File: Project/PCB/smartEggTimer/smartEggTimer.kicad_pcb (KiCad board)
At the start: 2 copper layers, 72 x 72 mm, 64 parts, among them J1 Conn_01x05_Pin, J2 Conn_01x02_Pin, J3 Conn_01x02_Pin, J4 Conn_01x06_Pin, J5 Conn_01x02_Socket, J6 Conn_01x02_Socket, J7 Conn_01x03_Pin, J8 Conn_01x03_Pin, Q1 STP60NF06L, SW1 SW_Push_Dual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

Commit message: rough positioning
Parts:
- C10, C11: footprint Capacitor_SMD:C_0603_1608Metric -> Capacitor_SMD:C_0805_2012Metric
- C12, C13, C7: footprint Capacitor_SMD:C_0805_2012Metric -> Capacitor_SMD:C_0402_1005Metric
- C15, C16, C17, C18, C8, C9: footprint Capacitor_SMD:C_0603_1608Metric -> Capacitor_SMD:C_0402_1005Metric
- SW1: value SW_Push_Dual -> SW_Push; footprint Button_Switch_THT:SW_PUSH_6mm_H9.5mm -> Button_Switch_THT:SW_PUSH_6mm
- SW3, SW4, SW5, SW6: value SW_Push_Dual -> SW_Push
- moved C14 105.4 mm to (125.6, 83.4), turned to -90 degrees
- moved C4 98.0 mm to (128.5, 91.4), turned to 90 degrees
- moved R14 97.7 mm to (121.4, 90.5)
- moved R12 97.5 mm to (124.5, 81.1), turned to 180 degrees
- moved R13 96.7 mm to (126.6, 81.1), turned to 180 degrees
- moved R15 96.6 mm to (121.5, 96.5), turned to 180 degrees
- moved C2 95.6 mm to (128.6, 97.4), turned to 90 degrees
- moved C5 89.1 mm to (140.3, 86.6)
- moved R17 87.0 mm to (129.7, 112.4), turned to -90 degrees
- moved C6 85.7 mm to (143.2, 90.4), turned to -90 degrees
- moved C3 84.5 mm to (139.5, 101.4), turned to 180 degrees
- moved C7 83.2 mm to (134.2, 86.5)
- moved R3 80.5 mm to (130.7, 82.1), turned to -90 degrees
- moved R16 80.2 mm to (136.3, 112.4), turned to 90 degrees
- moved C15 76.5 mm to (121.5, 97.7), turned to 180 degrees
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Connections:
- DFPlayerMini1 pad 3: /UART2_TX -> /USART2_RX
- J1 pad 3: /I2C_SCL -> /I2C1_SCL
- J3 pad 1: unconnected-(J3-Pin_1-Pad1) -> /USART3_TX
- J3 pad 2: unconnected-(J3-Pin_2-Pad2) -> /USART3_RX
- J4 pad 4: /I2C_SCL -> /I2C1_SCL
- OLED-15W-C1 pad 4: /I2C_SCL -> /I2C1_SCL
- R15 pad 2: Net-(R15-Pad2) -> Net-(R14-Pad1)
- R17 pad 2: Net-(R17-Pad2) -> Net-(R16-Pad1)
- R19 pad 2: Net-(R19-Pad2) -> Net-(R18-Pad1)
- R21 pad 2: Net-(R21-Pad2) -> Net-(R20-Pad1)
- R3 pad 2: /UART2_RX -> /USART2_TX
- R6 pad 1: /I2C1_SDA -> /I2C1_SCL
- R7 pad 1: /I2C_SCL -> /I2C1_SDA
- SW1 pad 1: /NRST -> GND
- SW3 pad 1: Net-(R14-Pad1) -> GND
- SW3 pad 2: Net-(R15-Pad2) -> Net-(R14-Pad1)
- SW4 pad 1: Net-(R16-Pad1) -> GND
- SW4 pad 2: Net-(R17-Pad2) -> Net-(R16-Pad1)
- SW5 pad 1: Net-(R18-Pad1) -> GND
- SW5 pad 2: Net-(R19-Pad2) -> Net-(R18-Pad1)
- SW6 pad 1: Net-(R20-Pad1) -> GND
- SW6 pad 2: Net-(R21-Pad2) -> Net-(R20-Pad1)
- U1 pad 16: unconnected-(U1-PA2-Pad16) -> /USART2_TX
- U1 pad 17: /UART2_RX -> /USART2_RX
- U1 pad 20: /UART2_TX -> unconnected-(U1-PA4-Pad20)
- U1 pad 51: unconnected-(U1-PC10-Pad51) -> /USART3_TX
- U1 pad 52: unconnected-(U1-PC11-Pad52) -> /USART3_RX
- U1 pad 58: /I2C1_SDA -> /I2C1_SCL
- U1 pad 59: /I2C_SCL -> /I2C1_SDA

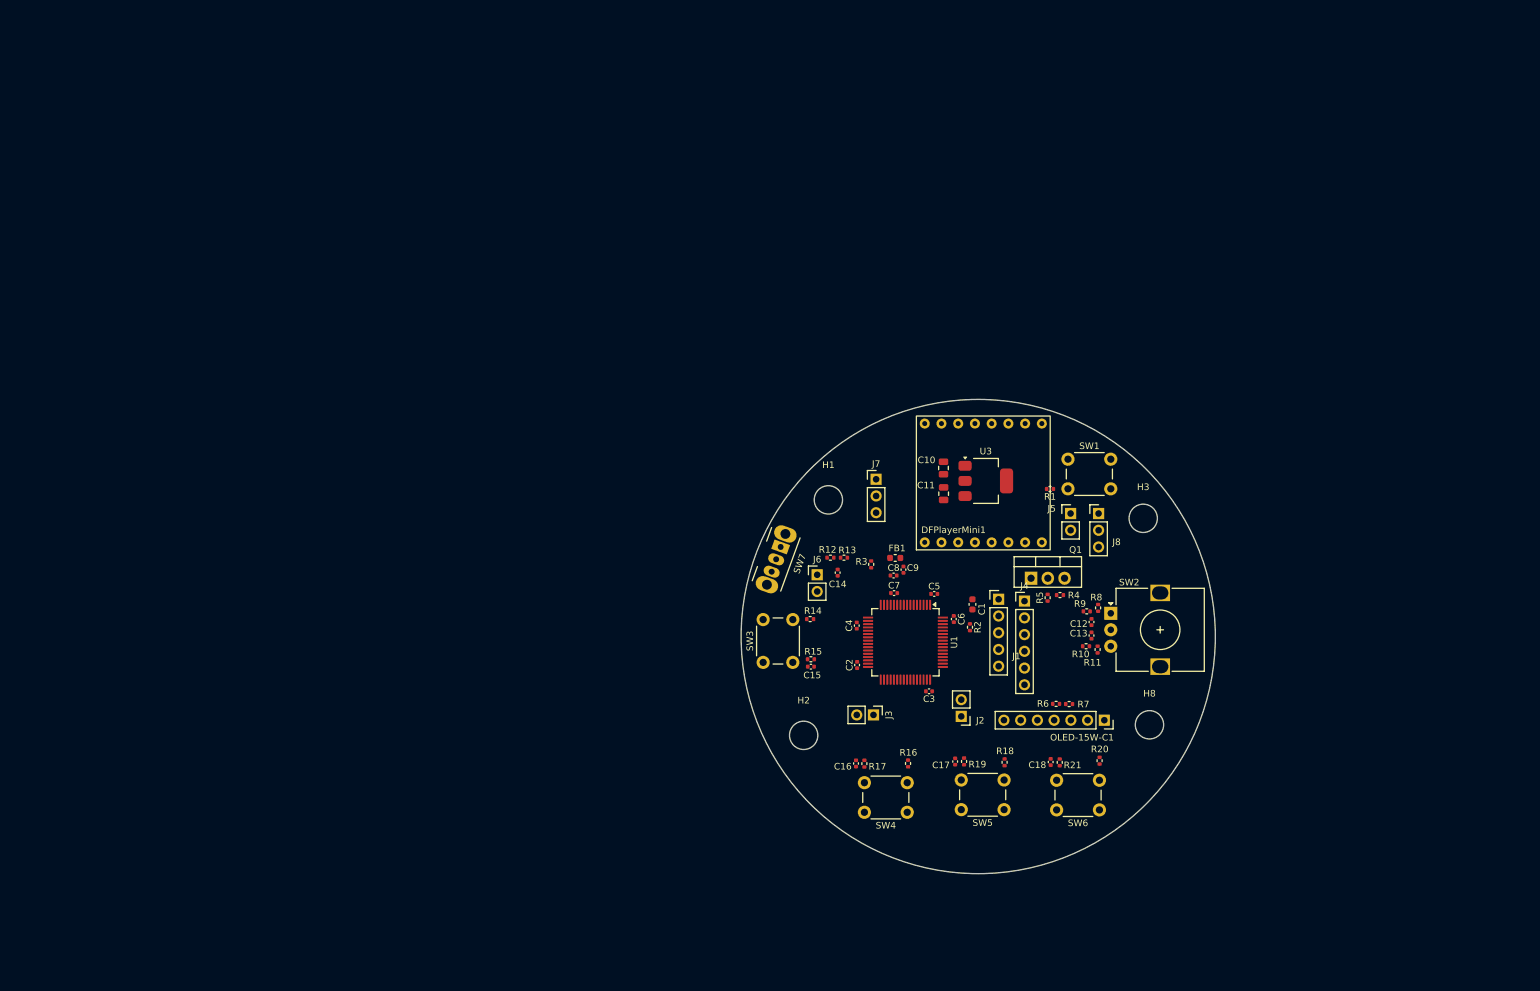
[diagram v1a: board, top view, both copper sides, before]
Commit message: add GND pins for SWD and optional UART
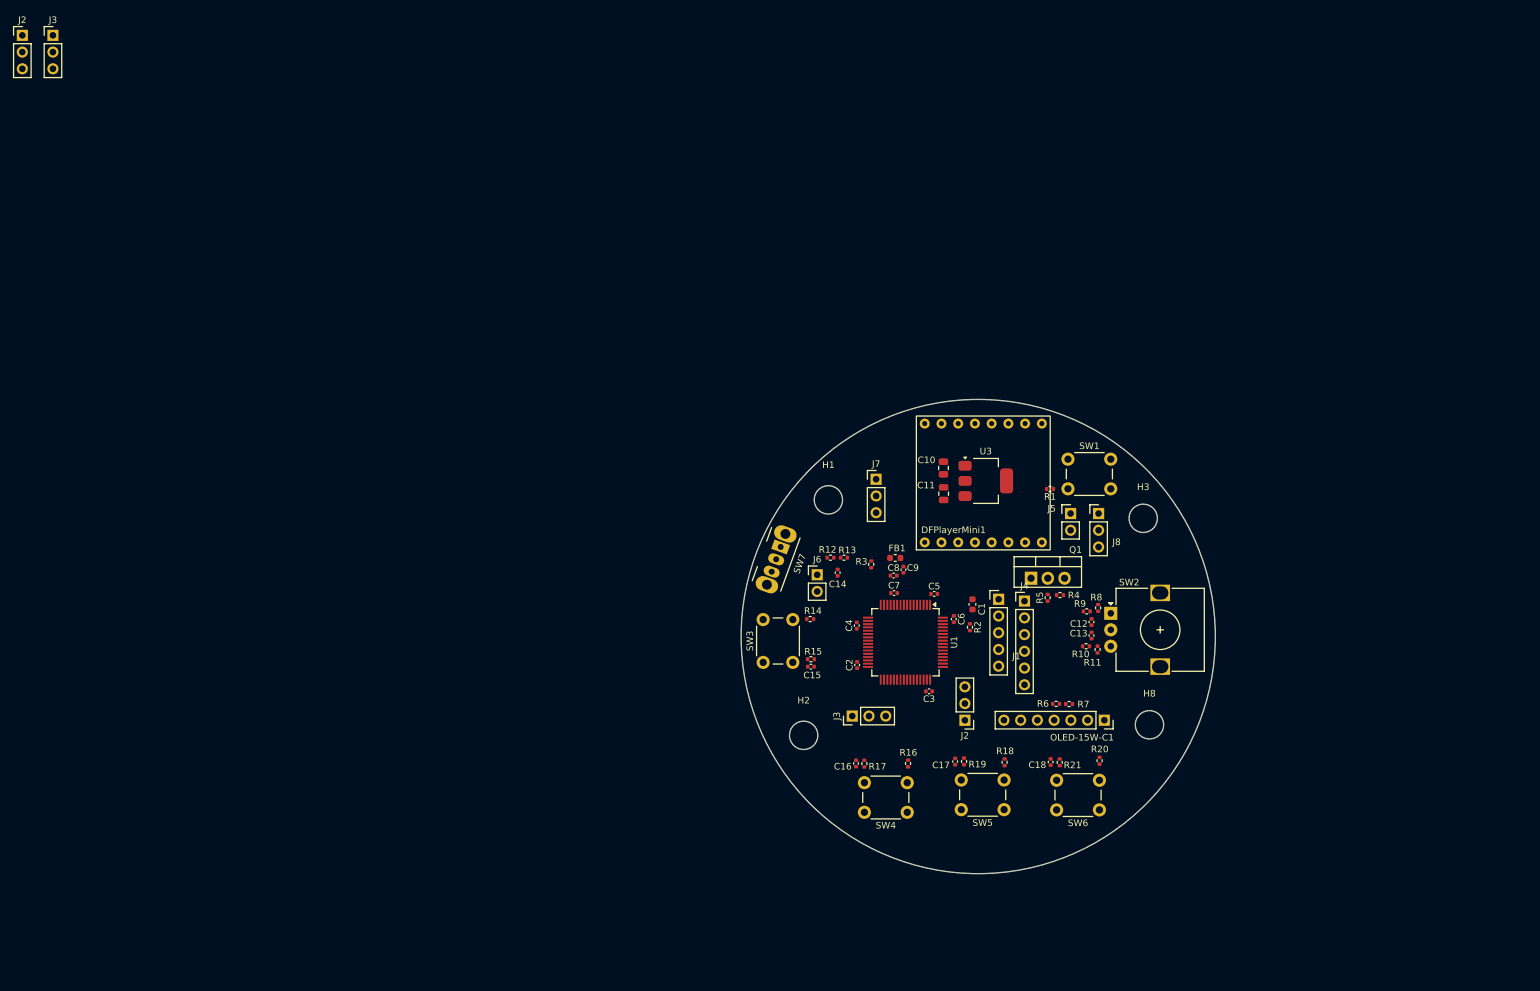
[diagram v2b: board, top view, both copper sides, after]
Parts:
- added J2: Conn_01x03_Pin, Connector_PinHeader_2.54mm:PinHeader_1x03_P2.54mm_Vertical, F.Cu at (1.82, 1.82)
- added J3: Conn_01x03_Pin, Connector_PinHeader_2.54mm:PinHeader_1x03_P2.54mm_Vertical, F.Cu at (6.47, 1.82)
- J2, J3: value Conn_01x02_Pin -> Conn_01x03_Pin; footprint Connector_PinHeader_2.54mm:PinHeader_1x02_P2.54mm_Vertical -> Connector_PinHeader_2.54mm:PinHeader_1x03_P2.54mm_Vertical
- moved J3 3.23 mm to (127.8, 105.2), turned to 90 degrees
- moved J2 0.81 mm to (144.9, 105.8)

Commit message: add exact positioning of critical parts (switches, rotary encoder and drill holes need to fit to the 3D design of the case)
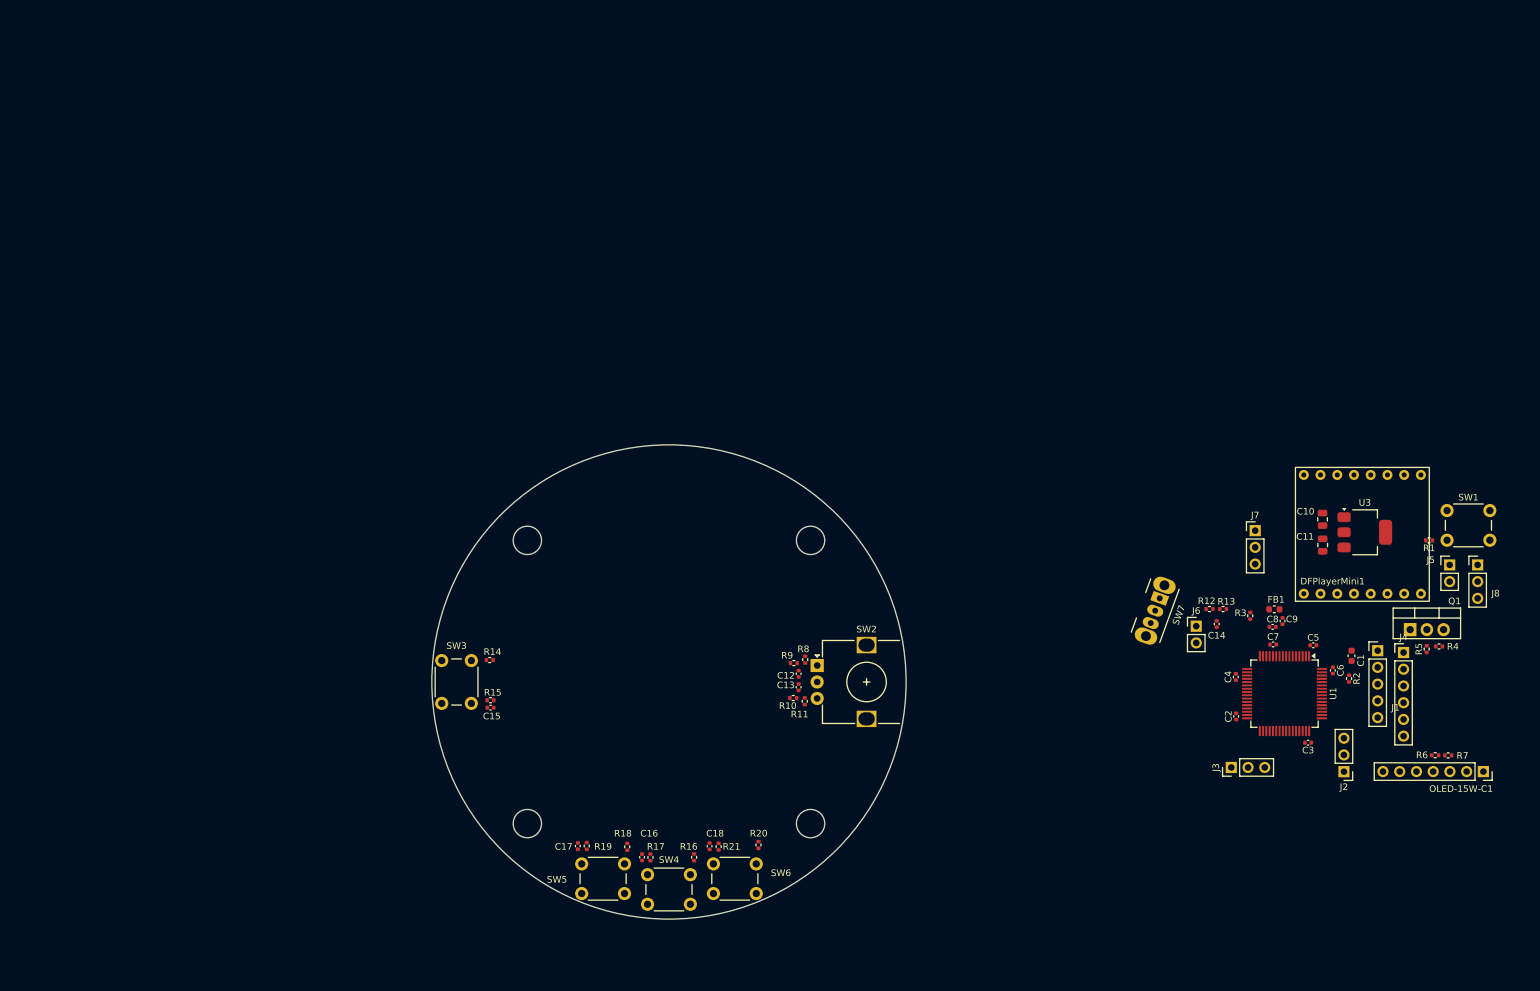
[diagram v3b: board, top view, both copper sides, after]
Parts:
- removed the J2 at (1.82, 1.82)
- removed the J3 at (6.47, 1.82)
- moved H3 104.4 mm to (78.5, 121.5)
- moved SW5 61.8 mm to (90.0, 129.9)
- moved R18 58.7 mm to (93.7, 125.0)
- moved R19 58.7 mm to (87.5, 124.9)
- moved C17 58.7 mm to (86.2, 124.9)
- moved C1 58.1 mm to (203.6, 96.0)
- moved C11 58.1 mm to (199.2, 79.2)
- moved C2 58.1 mm to (186.1, 105.2)
- moved C3 58.1 mm to (197.0, 109.2)
- moved C4 58.1 mm to (186.1, 99.2)
- moved C5 58.1 mm to (197.8, 94.4)
- moved C6 58.1 mm to (200.8, 98.2)
- moved C7 58.1 mm to (191.7, 94.3)
- moved C8 58.1 mm to (191.7, 91.6)
- moved C9 58.1 mm to (193.2, 90.7)
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
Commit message: rework DFPlayer section based on prototyping - add pull-up resistors for UART communication - add a pin header for the input voltage
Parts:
- removed R3: 1k, Resistor_SMD:R_0402_1005Metric
- added J9: Conn_01x02_Pin, Connector_PinHeader_2.54mm:PinHeader_1x02_P2.54mm_Vertical, F.Cu at (224.7, 104.3)
- added R22: 100k, Resistor_SMD:R_0402_1005Metric, F.Cu at (228.5, 103.0)
- added R23: 100k, Resistor_SMD:R_0402_1005Metric, F.Cu at (228.5, 105.0)
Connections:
- DFPlayerMini1 pad 1: /Battery-SW -> Net-(DFPlayerMini1-VCC)
- DFPlayerMini1 pad 2: Net-(DFPlayerMini1-RX) -> /USART2_TX

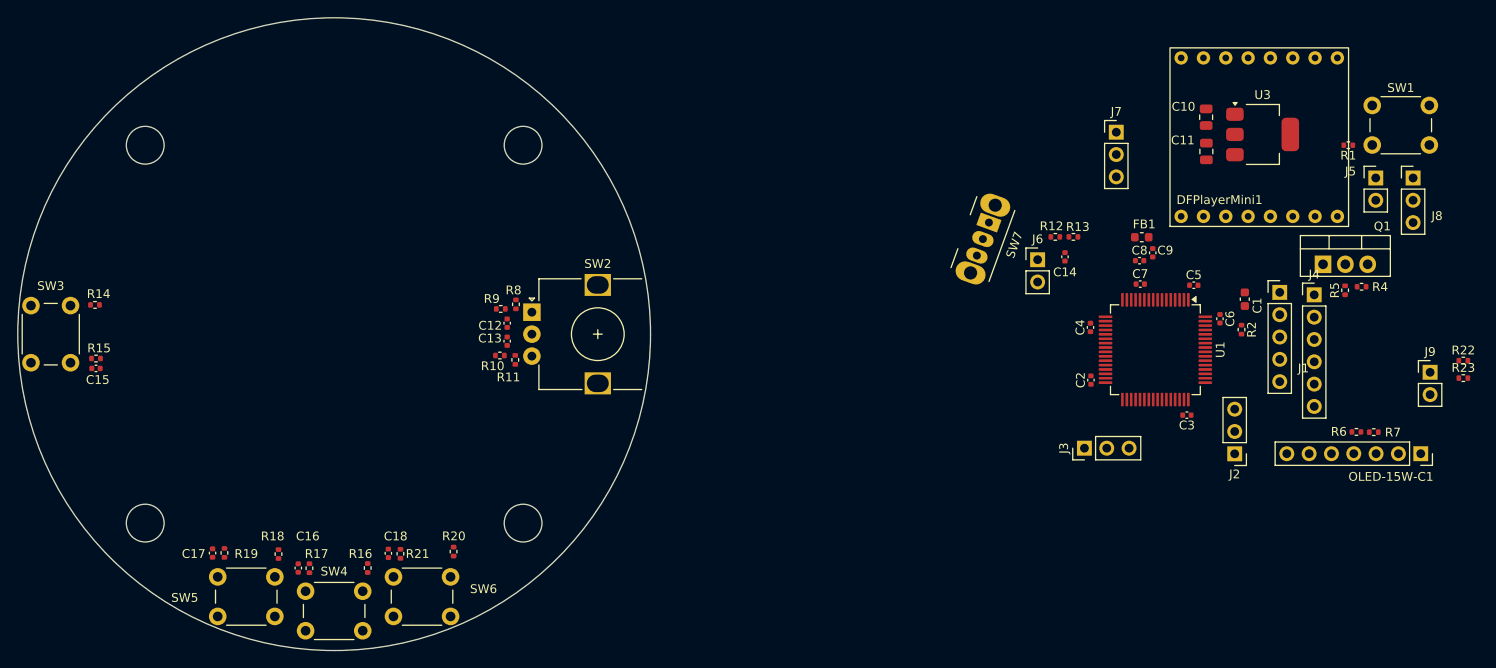
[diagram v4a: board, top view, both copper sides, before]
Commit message: placement of all components & initial routing
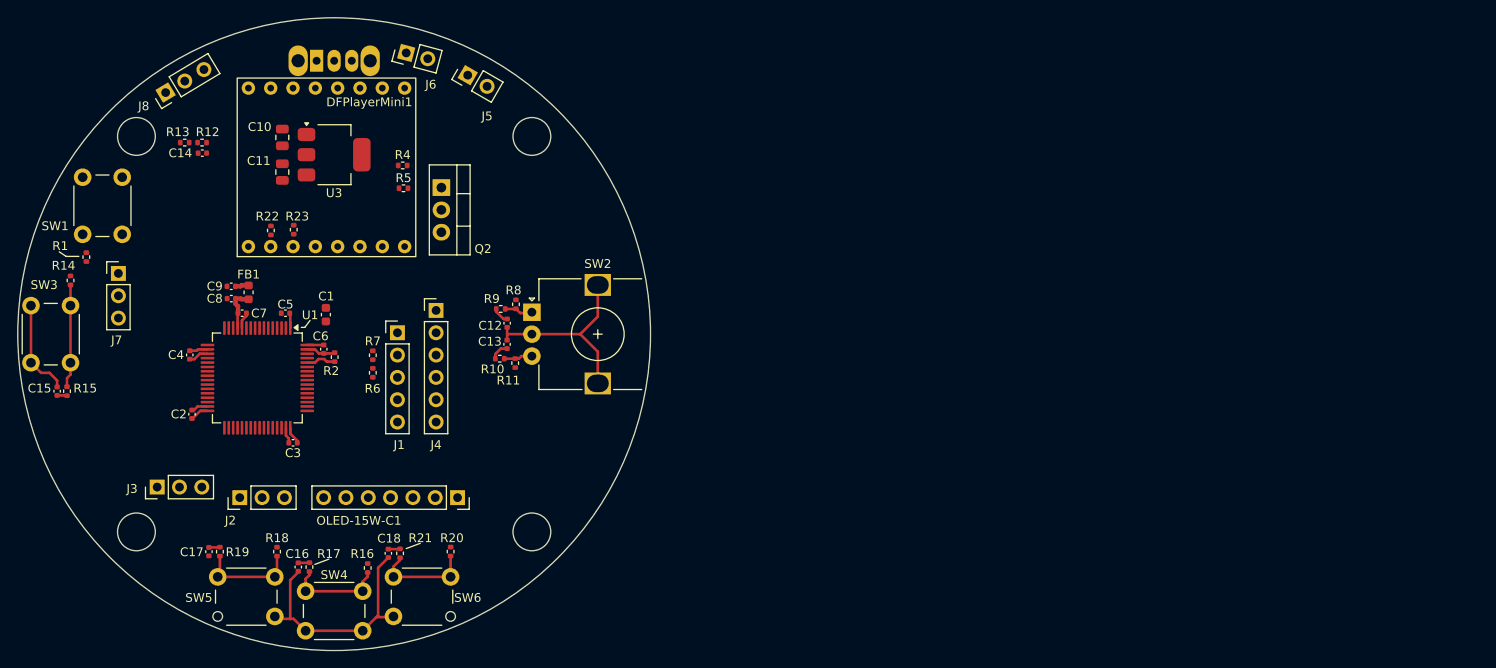
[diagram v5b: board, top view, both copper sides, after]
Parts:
- removed J9: Conn_01x02_Pin, Connector_PinHeader_2.54mm:PinHeader_1x02_P2.54mm_Vertical
- removed Q1: STP60NF06L, Package_TO_SOT_THT:TO-220-3_Vertical
- added Q2: STP60NF06L, Package_TO_SOT_THT:TO-220-3_Vertical, F.Cu at (112.2, 83.3)
- SW7: moved to B.Cu
- moved SW1 147.5 mm to (71.4, 88.6), turned to 90 degrees
- moved R1 144.2 mm to (71.8, 91.2), turned to -90 degrees
- moved J8 142.3 mm to (80.8, 72.5), turned to 121 degrees
- moved R22 136.5 mm to (92.8, 88.2), turned to -90 degrees
- moved R23 134.2 mm to (95.4, 88.1), turned to -90 degrees
- moved J7 114.7 mm to (75.5, 93.1)
- moved R7 114.2 mm to (104.4, 102.4), turned to -90 degrees
- moved J2 113.3 mm to (89.3, 118.6), turned to 90 degrees
- moved R6 112.1 mm to (104.4, 104.4), turned to 90 degrees
- moved R4 110.0 mm to (107.8, 80.8), turned to 180 degrees
- moved OLED-15W-C1 109.7 mm to (114.0, 118.6)
- moved R5 107.8 mm to (107.9, 83.4), turned to 0 degrees
- moved DFPlayerMini1 106.2 mm to (99.1, 81.0)
- moved U3 105.7 mm to (100.0, 79.6)
- moved J3 105.6 mm to (79.9, 117.4)
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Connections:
- DFPlayerMini1 pad 1: Net-(DFPlayerMini1-VCC) -> /Battery-SW
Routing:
- net GND: track 0.00 -> 72.8 mm
- net Net-(R14-Pad1): track 0.00 -> 11.7 mm
- net +3.3V: track 0.00 -> 11.6 mm
- net Net-(R18-Pad1): track 0.00 -> 11.4 mm
- net Net-(R20-Pad1): track 0.00 -> 11.4 mm
- net Net-(R16-Pad1): track 0.00 -> 11.3 mm
- net +3.3VA: track 0.00 -> 5.00 mm
- net /BOOT0: track 0.00 -> 3.41 mm
- net Net-(R8-Pad2): track 0.00 -> 3.28 mm
- net Net-(R10-Pad1): track 0.00 -> 3.26 mm
- net /Rotary Encoder b: track 0.00 -> 2.12 mm
- net /Rotary Encoder a: track 0.00 -> 1.89 mm
- net /Button_4: track 0.00 -> 1.35 mm
- net /Button_3: track 0.00 -> 1.28 mm
- net /Button_2: track 0.00 -> 1.26 mm
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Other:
- board text added: "On"
- board text added: "important measurements: - diameter of the PCB has to be 72mm - there are 4 mounting holes, each 22.5mm away in both directions from the center - the center of the rotary encoder has to be 30mm away from the center - the three buttons on the bottom sit on a circle with a diameter of 63mm, the center of the buttons should sit directly on this circle, the horizontal distance between the centers of t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"
- board text removed: "diameter of the PCB has to be 72mm with 4 holes, each 21.5mm in both direction from the center away The center of the rotary encoder has to be 30mm from the center away the 4 buttons also have a fixed position as soon as we finished the CAD model"
